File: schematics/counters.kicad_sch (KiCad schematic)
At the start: 28 parts, among them U10 74HC390, U11 74HC390, U12 74HC390, U13 ATF22V10C, U4 74HC08, U5 74HC08, U6 74HC4046, U7 74HC86, U8 74HC390, U9 74HC390

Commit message: started a second version
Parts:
- R12: value 10K -> 7K5
- R37: value 100K -> 220K
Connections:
- net CS0: now also U9.3 (1Q_{A}), U9.4 (1~{CLK}_{B}); no longer U9.12 (2~{CLK}_{B}), U9.13 (2Q_{A})
- net CS1: now also U9.5 (1Q_{B}); no longer U9.11 (2Q_{B})
- net CS2: now also U9.6 (1Q_{C}); no longer U9.10 (2Q_{C})
- net CS3: now also U9.15 (2~{CLK}_{A}), U9.7 (1Q_{D}); no longer U9.1 (1~{CLK}_{A}), U9.9 (2Q_{D})
- net DS0: now also U9.12 (2~{CLK}_{B}), U9.13 (2Q_{A}); no longer U9.3 (1Q_{A}), U9.4 (1~{CLK}_{B})
- net DS1: now also U9.11 (2Q_{B}); no longer U9.5 (1Q_{B})
- net DS2: now also U4.10, U4.13, U9.10 (2Q_{C}); no longer U9.6 (1Q_{C})
- net DS3: now also U9.9 (2Q_{D}); no longer U4.10, U4.13, U9.7 (1Q_{D})
- net GND: now also R16.2, U12.15 (2~{CLK}_{A}); no longer R16.1
- net REFCLK: now also U6.3 (COMP_{IN}); no longer U6.14 (SIG_{IN})
- net at U12.10 (2Q_{C}): now also U13.13 (I_{11}), U4.2
- net at U12.7 (1Q_{D}), U13.9 (I_{8}): now also U12.12 (2~{CLK}_{B}); no longer U12.15 (2~{CLK}_{A})
- net at D10.1 (K), D11.1 (K), U10.14 (2CLR): now also R16.1; no longer R16.2
- net at U8.7 (1Q_{D}): now also U6.14 (SIG_{IN}); no longer U8.1 (1~{CLK}_{A})
- net SEL1: now reaches U8.3 (1Q_{A})
- net SEL1: now also U8.12 (2~{CLK}_{B}), U8.15 (2~{CLK}_{A}), U8.4 (1~{CLK}_{B}); no longer U6.3 (COMP_{IN})
- net at U5.8, U8.14 (2CLR): now also U9.1 (1~{CLK}_{A}); no longer U9.15 (2~{CLK}_{A})
- net ~{HHSEL}: now reaches U13.5 (I_{4})
- removed net S0: U6.4 (VCO_{OUT}), U8.15 (2~{CLK}_{A}), U8.4 (1~{CLK}_{B})
- net S1 renamed SEL2
- net SEL2: no longer U8.12 (2~{CLK}_{B})
- new net: U12.11 (2Q_{B}), U13.10 (I_{9})
- new net SEL0: U6.4 (VCO_{OUT}), U8.1 (1~{CLK}_{A})
- now unconnected: U12.13 (2Q_{A})
- no-connect marks 19 -> 18
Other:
- note added: "0.1Hz"
- note added: "1/10min"
- note added: "1/day"
- note added: "1/hr"
- note added: "1/min"
- note added: "10Hz"
- note added: "2Hz"
- note removed: "1/hour"
- note removed: "1/minute"
- note removed: "digit pair select"
- moved on the sheet: C13, C14, C15, C16, C17, C19, C20, C21, C22, C23, C24, C25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

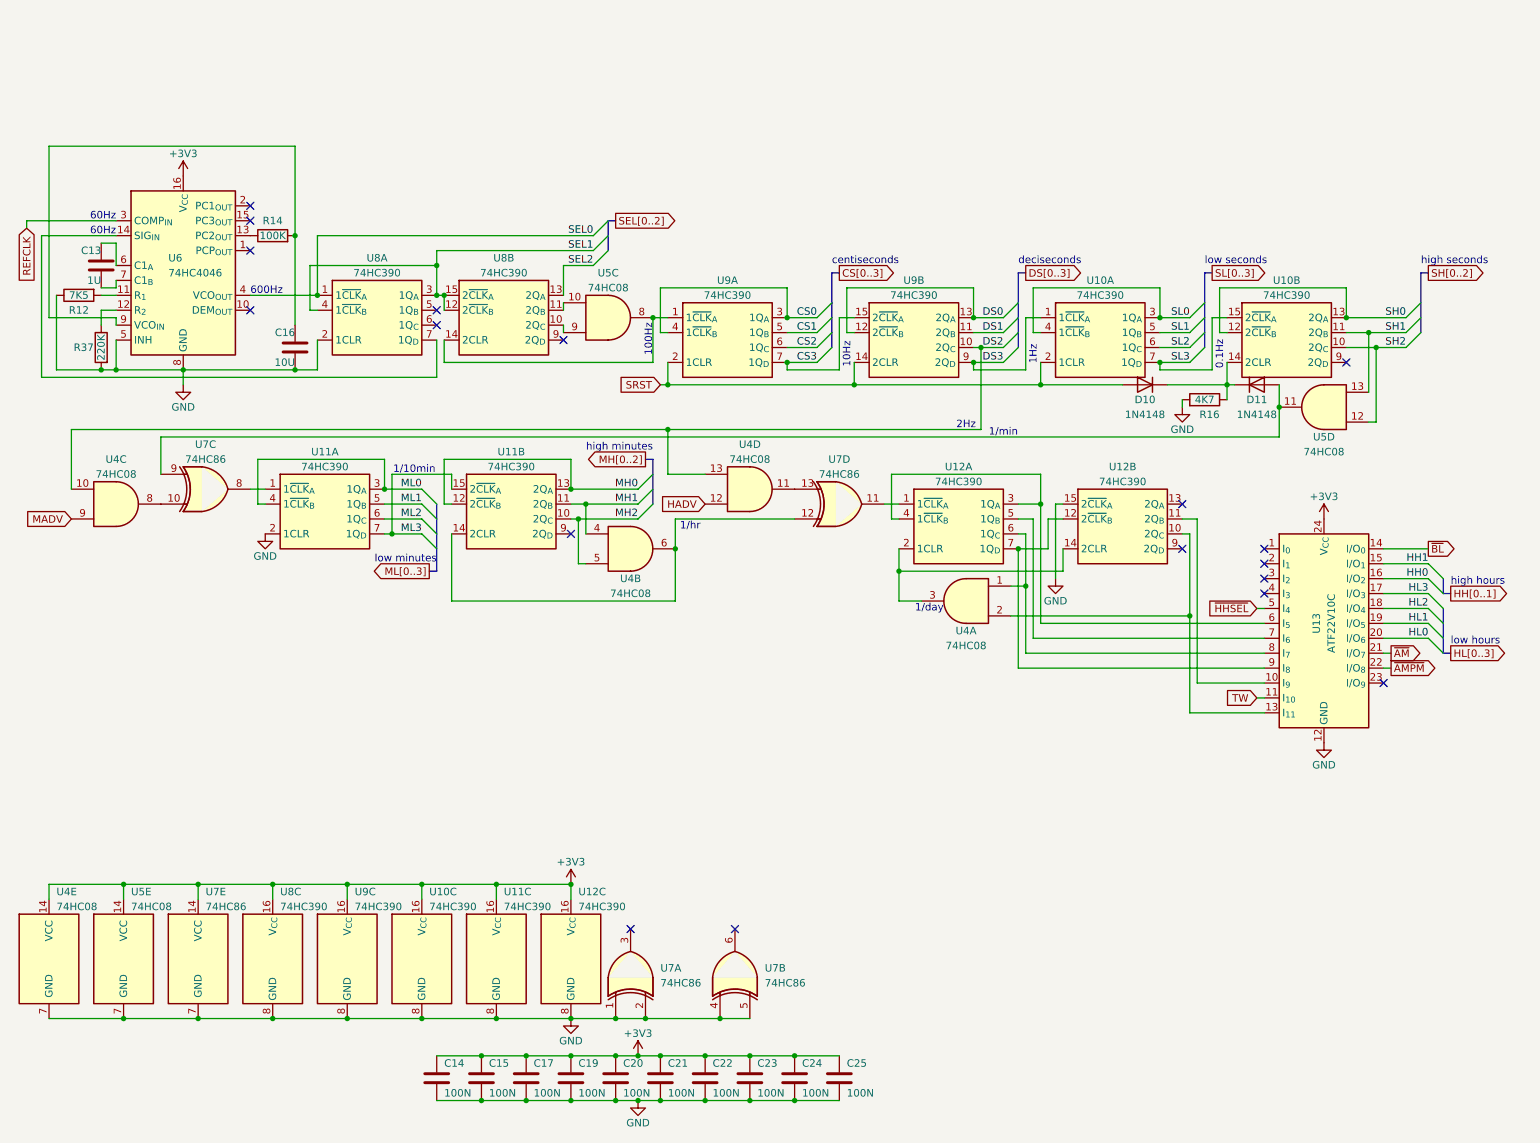
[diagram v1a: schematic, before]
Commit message: switched to diode logic; added LED dimmer
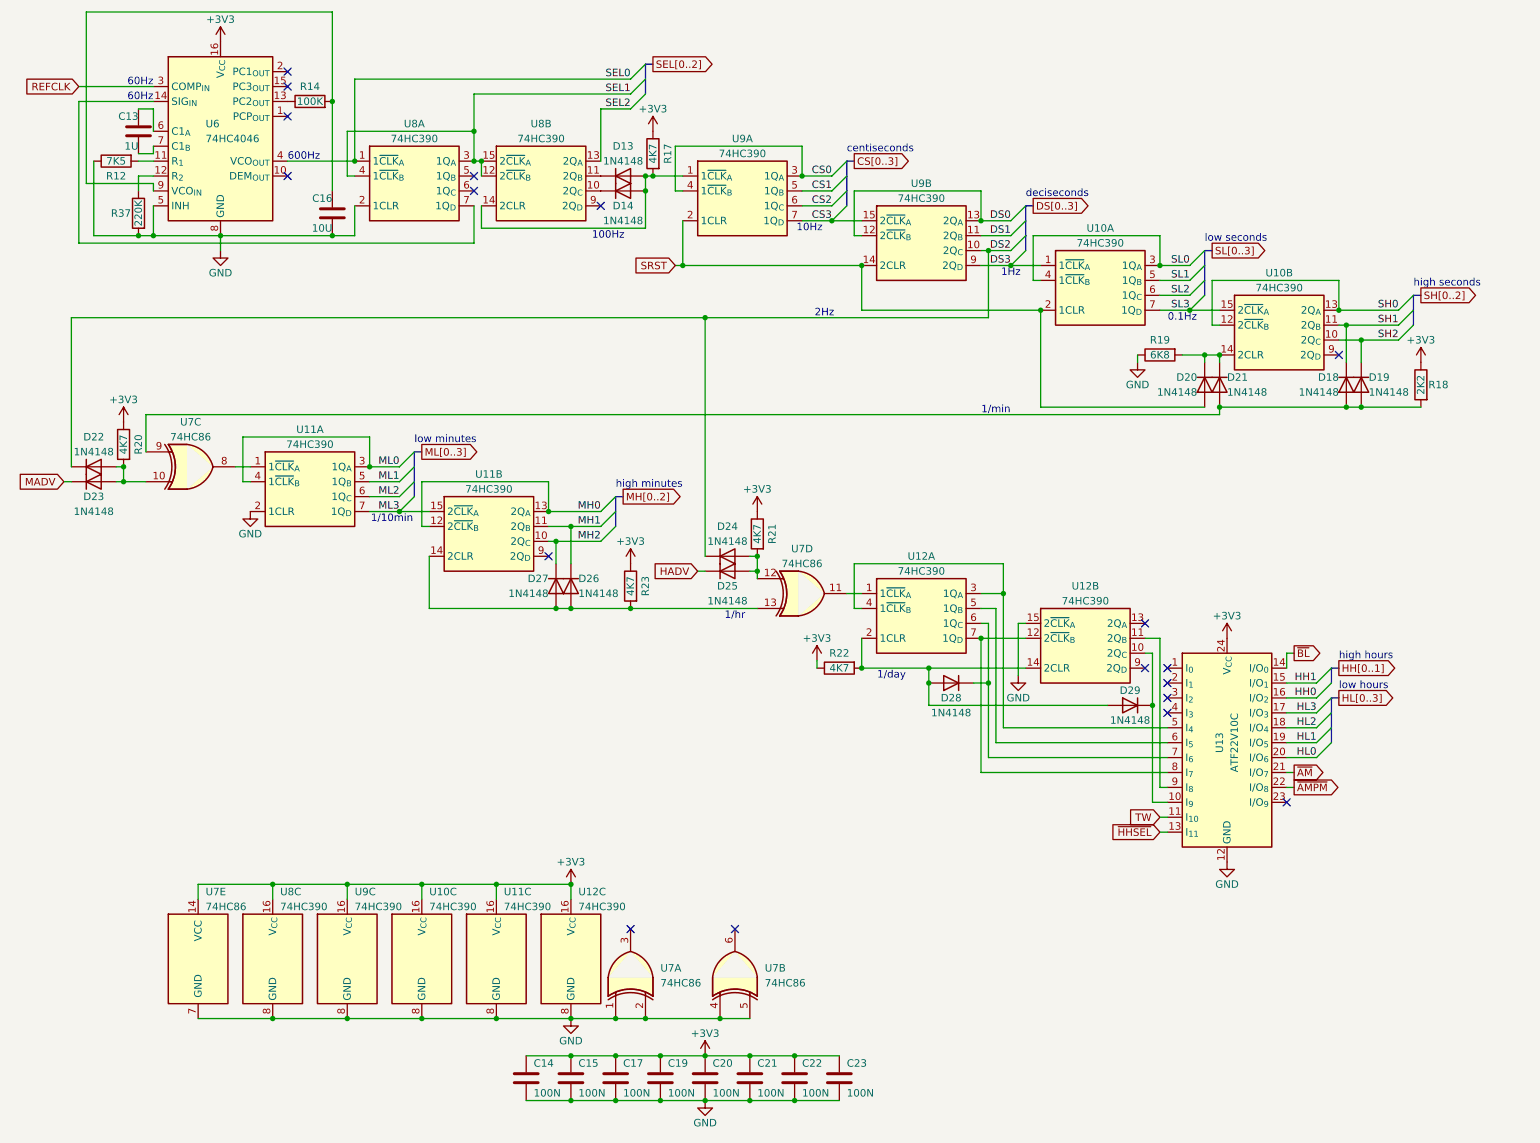
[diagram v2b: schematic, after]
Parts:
- removed C24, C25: 100N, Package_SO:SOIC-8_3.9x4.9mm_P1.27mm, symbol Device:C
- removed D10, D11: 1N4148, Diode_THT:D_DO-35_SOD27_P7.62mm_Horizontal, symbol Diode:1N4148
- removed R16: 4K7, symbol Device:R
- removed U4, U5: 74HC08, Package_TO_SOT_SMD:SC-74A-5_1.55x2.9mm_P0.95mm, symbol 74xx:74LS08
- added D13, D14, D18, D19, D20, D21, D22, D23, D24, D25, D26, D27, D28, D29: 1N4148, Diode_THT:D_DO-35_SOD27_P7.62mm_Horizontal, symbol Diode:1N4148
- added R17, R20, R21, R22, R23: 4K7, symbol Device:R
- added R18: 2K2, symbol Device:R
- added R19: 6K8, symbol Device:R
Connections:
- net +3V3: now also R17.1, R18.1, R20.1, R21.1, R22.1, R23.1
- net DS2: now also D22.1 (K), D24.1 (K)
- net GND: now also R19.1
- net HADV: now also D25.1 (K)
- net MADV: now also D23.1 (K)
- net MH1: now also D26.1 (K)
- net MH2: now also D27.1 (K)
- net SH1: now also D18.1 (K)
- net SH2: now also D19.1 (K)
- net SRST: now also D20.2 (A)
- net ~{HHSEL}: now also U13.13 (I_{11}); no longer U13.5 (I_{4})
- net at U11.14 (2CLR): now also U7.13, D26.2 (A), D27.2 (A), R23.2; no longer U7.12
- net at U7.9: now also D18.2 (A), D19.2 (A), D21.2 (A), R18.2
- net at U8.14 (2CLR), U9.1 (1~{CLK}_{A}): now also D13.2 (A), D14.2 (A), R17.2
- net at U12.10 (2Q_{C}): now also U13.10 (I_{9}), D29.1 (K); no longer U13.13 (I_{11})
- net at U12.11 (2Q_{B}): now also U13.9 (I_{8}); no longer U13.10 (I_{9})
- net at U12.12 (2~{CLK}_{B}), U12.7 (1Q_{D}): now also U13.8 (I_{7}); no longer U13.9 (I_{8})
- net at U12.14 (2CLR), U12.2 (1CLR): now also D28.2 (A), D29.2 (A), R22.2
- net at U12.3 (1Q_{A}), U12.4 (1~{CLK}_{B}): now also U13.5 (I_{4}); no longer U13.6 (I_{5})
- net at U13.7 (I_{6}): now also U12.6 (1Q_{C}), D28.1 (K); no longer U12.5 (1Q_{B})
- net at U7.10: now also D22.2 (A), D23.2 (A), R20.2
- net at U10.14 (2CLR): now also D20.1 (K), D21.1 (K), R19.2
- net at U8.10 (2Q_{C}): now also D14.1 (K)
- net at U8.11 (2Q_{B}): now also D13.1 (K)
- new net: D24.2 (A), D25.2 (A), R21.2, U7.12
- new net: U12.5 (1Q_{B}), U13.6 (I_{5})
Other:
- moved on the sheet: C13, C14, C15, C16, C17, C19, C20, C21, C22, C23, R12, R14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

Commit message: re-annotate
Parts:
- renumbered C13 to C10, C16 to C11, C14 to C12, C15 to C13, C17 to C14, C19 to C15, C20 to C16, C21 to C17, C22 to C18, C23 to C19, D22 to D10, D23 to D11, D27 to D12, D26 to D13, D13 to D14, D14 to D15, D24 to D16, D25 to D17, D28 to D18, D29 to D19, D18 to D22, D19 to D23, R20 to R13, R37 to R14, R14 to R15, R23 to R16, R21 to R18, R22 to R19, R19 to R20, R18 to R21, U12 to U10, U13 to U11, U7 to U4, U6 to U5, U8 to U6, U11 to U7, U9 to U8, U10 to U9

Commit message: diode matrix rom
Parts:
- removed U11: ATF22V10C, Package_DIP:DIP-24_W7.62mm, symbol Logic_Programmable:PAL22V10-xxP
- R20: value 6K8 -> 10K
- R21: value 2K2 -> 1K
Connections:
- net HI2: now reaches D18.1 (K), U10.6 (1Q_{C})
- net HI4: now reaches D19.1 (K)
- net HI4: now also U10.11 (2Q_{B}); no longer U10.10 (2Q_{C})
- net HI3: now reaches U10.12 (2~{CLK}_{B}), U10.7 (1Q_{D})
- net HI0: now reaches U10.3 (1Q_{A}), U10.4 (1~{CLK}_{B})
- net HI1: now reaches U10.5 (1Q_{B})
- new net HI5: U10.10 (2Q_{C})
- no-connect marks 18 -> 13
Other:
- note added: "hours input"
- note removed: "high hours"
- note removed: "low hours"
- moved on the sheet: D19, U10B

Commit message: 24-12 converter cleanup
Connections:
- net DS0: now also U10.15 (2~{CLK}_{A})
- net DS2: no longer D10.1 (K), D16.1 (K)
- net GND: no longer U10.15 (2~{CLK}_{A})
- net SRST: now also D20.1 (K); no longer D20.2 (A)
- net at D22.2 (A), D23.2 (A), R21.2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: now also D21.1 (K); no longer D21.2 (A)
- net at R20.2, U9.14 (2CLR): now also D20.2 (A), D21.2 (A); no longer D20.1 (K), D21.1 (K)
- net at U10.13 (2Q_{A}): now also D10.1 (K), D16.1 (K)
- no-connect marks 13 -> 12
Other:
- note added: "2.5Hz (for setting)"
- note removed: "2Hz"
- moved on the sheet: C10, C11, D10, D11, D12, D13, D14, D15, D16, D17, D18, D19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

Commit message: added some PCB footprints
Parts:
- C10, C11, C12, C13, C14, C15, C16, C17, C18, C19: footprint Package_SO:SOIC-8_3.9x4.9mm_P1.27mm -> Capacitor_THT:C_Disc_D5.1mm_W3.2mm_P5.00mm
- R12, R15, R16, R17, R18, R19, R20, R21: footprint (none) -> Resistor_THT:R_Axial_DIN0207_L6.3mm_D2.5mm_P10.16mm_Horizontal
- R13: renamed from R14; footprint (none) -> Resistor_THT:R_Axial_DIN0207_L6.3mm_D2.5mm_P10.16mm_Horizontal
- R14: renamed from R13; footprint (none) -> Resistor_THT:R_Axial_DIN0207_L6.3mm_D2.5mm_P10.16mm_Horizontal
- U10, U6: footprint Package_TO_SOT_THT:TO-92_Inline -> Package_DIP:DIP-16_W7.62mm
- U4: footprint (none) -> Package_DIP:DIP-14_W7.62mm
- U5: footprint Package_LCC:PLCC-84_29.3x29.3mm_P1.27mm -> Package_DIP:DIP-16_W7.62mm
- U7: renamed from U8; footprint Package_TO_SOT_THT:TO-92_Inline -> Package_DIP:DIP-16_W7.62mm
- U8: renamed from U9; footprint Package_TO_SOT_THT:TO-92_Inline -> Package_DIP:DIP-16_W7.62mm
- U9: renamed from U7; footprint Package_TO_SOT_THT:TO-92_Inline -> Package_DIP:DIP-16_W7.62mm
- renumbered D14 to D12, D15 to D13, D12 to D14, D13 to D15, D20 to D19, D21 to D20, D19 to D21

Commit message: switched to PWM for LEDs
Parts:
- removed C19: 100N, Capacitor_THT:C_Disc_D5.1mm_W3.2mm_P5.00mm, symbol Device:C
- removed R14, R16, R17, R18, R19: 4K7, Resistor_THT:R_Axial_DIN0207_L6.3mm_D2.5mm_P10.16mm_Horizontal, symbol Device:R
- added C30, C8: 100N, Capacitor_THT:C_Disc_D5.1mm_W3.2mm_P5.00mm, symbol Device:C
- added C6: 10N, Capacitor_THT:C_Disc_D5.1mm_W3.2mm_P5.00mm, symbol Device:C
- added D7: BAT43, Diode_THT:D_DO-35_SOD27_P7.62mm_Horizontal, symbol Device:D_Schottky
- added Q18: S8050, Package_TO_SOT_THT:TO-92_HandSolder, symbol Transistor_BJT:Q_NPN_EBC
- added R34, R36: 4K7, Resistor_THT:R_Axial_DIN0207_L6.3mm_D2.5mm_P7.62mm_Horizontal, symbol Device:R
- added R35: 47K, Resistor_THT:R_Axial_DIN0207_L6.3mm_D2.5mm_P7.62mm_Horizontal, symbol Device:R
- added R37: 12K, Resistor_THT:R_Axial_DIN0207_L6.3mm_D2.5mm_P7.62mm_Horizontal, symbol Device:R
- added R38: 150R, Resistor_THT:R_Axial_DIN0207_L6.3mm_D2.5mm_P7.62mm_Horizontal, symbol Device:R
- added R39: 1K5, Resistor_THT:R_Axial_DIN0207_L6.3mm_D2.5mm_P7.62mm_Horizontal, symbol Device:R
- added RN2: 4K7, Resistor_THT:R_Array_SIP9, symbol Device:R_Network08_Split
- added RV1: 5K, bvclock:Bourns_3362P_Trimming_Potentiometer, symbol Device:R_Potentiometer_Trim
- added U1: 74HC14, Package_DIP:DIP-14_W7.62mm, symbol 74xx:74HC14
- added U3: LMC555xN, Package_DIP:DIP-8_W7.62mm, symbol Timer:LMC555xN
- R10: renamed from R15; footprint Resistor_THT:R_Axial_DIN0207_L6.3mm_D2.5mm_P10.16mm_Horizontal -> Resistor_THT:R_Axial_DIN0207_L6.3mm_D2.5mm_P7.62mm_Horizontal
- R11: renamed from R20; footprint Resistor_THT:R_Axial_DIN0207_L6.3mm_D2.5mm_P10.16mm_Horizontal -> Resistor_THT:R_Axial_DIN0207_L6.3mm_D2.5mm_P7.62mm_Horizontal
- R12: renamed from R21; footprint Resistor_THT:R_Axial_DIN0207_L6.3mm_D2.5mm_P10.16mm_Horizontal -> Resistor_THT:R_Axial_DIN0207_L6.3mm_D2.5mm_P7.62mm_Horizontal
- R8: renamed from R12; footprint Resistor_THT:R_Axial_DIN0207_L6.3mm_D2.5mm_P10.16mm_Horizontal -> Resistor_THT:R_Axial_DIN0207_L6.3mm_D2.5mm_P7.62mm_Horizontal
- R9: renamed from R13; footprint Resistor_THT:R_Axial_DIN0207_L6.3mm_D2.5mm_P10.16mm_Horizontal -> Resistor_THT:R_Axial_DIN0207_L6.3mm_D2.5mm_P7.62mm_Horizontal
- renumbered D20 to D19, D19 to D20
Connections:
- net +3V3: now also C30.1, R34.1, R37.1, R39.1, RN2.1 (R1), RN2.1 (R1), RN2.1 (R1), RN2.1 (R1), U3.4 (~{RST}), U3.8 (VCC)
- net GND: now also C30.2, C8.2, D7.2 (A), Q18.1 (E), R36.2, RV1.3, U3.1 (GND)
- net SEL0: now also U1.3
- net SRST: now also D19.2 (A); no longer D20.1 (K)
- net at D14.2 (A), D15.2 (A), U4.13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: now also RN2.8 (R7.2)
- net at D16.2 (A), D17.2 (A), U4.12: now also RN2.7 (R6.2)
- net at D22.2 (A), D23.2 (A), R12.2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: now also D20.2 (A); no longer D19.1 (K)
- net at R11.2, U8.14 (2CLR): now also D19.1 (K), D20.1 (K); no longer D19.2 (A), D20.2 (A)
- net at D12.2 (A), D13.2 (A), U6.14 (2CLR)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: now also R34.2
- net at D18.2 (A), D21.2 (A), U10.14 (2CLR)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: now also RN2.6 (R5.2)
- net at D10.2 (A), D11.2 (A), U4.10: now also RN2.9 (R8.2)
- new net: C6.1, U1.4
- new net: C6.2, R35.1, R36.1
- new net: U1.6, U3.2 (TRIG)
- new net: R38.1, U3.3 (OUT)
- new net: RV1.2, U3.5 (CONT)
- new net: C8.1, R37.2, U3.6 (THRES), U3.7 (DISCH)
- new net: R39.2, RV1.1
- new net: D7.1 (K), R35.2, U1.5
- new net: Q18.2 (B), R38.2
- new net VEE: Q18.3 (C)
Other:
- moved on the sheet: D19, D20

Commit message: fiddled with transistors
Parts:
- R14: renamed from R38; value 150R -> 100R
- renumbered C11 to C10, C8 to C11, C30 to C19, C6 to C8, C10 to C9, D11 to D10, D12 to D11, D13 to D12, D14 to D13, D15 to D14, D16 to D15, D17 to D16, D18 to D17, D19 to D18, D20 to D19, D21 to D20, D22 to D21, D23 to D22, D7 to D8, D10 to D9, Q18 to Q1, R35 to R10, R39 to R11, R10 to R12, R37 to R13, R34 to R15, R11 to R16, R12 to R17, R8 to R7, R9 to R8, R36 to R9, U4 to U3, U5 to U4, U6 to U5, U7 to U6, U8 to U7, U3 to U8
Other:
- note added: "253.75mA"
